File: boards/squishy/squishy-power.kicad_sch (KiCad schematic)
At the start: 63 parts, among them SW1 RST, U1 LFE5UM5G-45F-8BG381C, U10 TPS720115QDRVRQ1, U16 LP5910-1.8DRVR, U2 W25N01GVZEIG, U5 APX811-40UG-7, U7 TPS73733DRVR, U8 TPS7A1125PDRVT, U9 TPS7A1112PDRVT

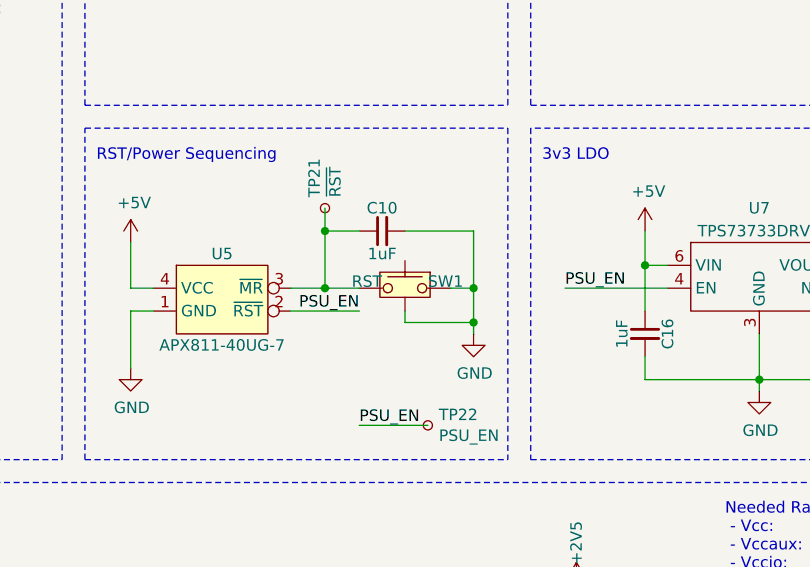
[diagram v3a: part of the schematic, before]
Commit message: hardware: squishy: some more minor work on the USB FE
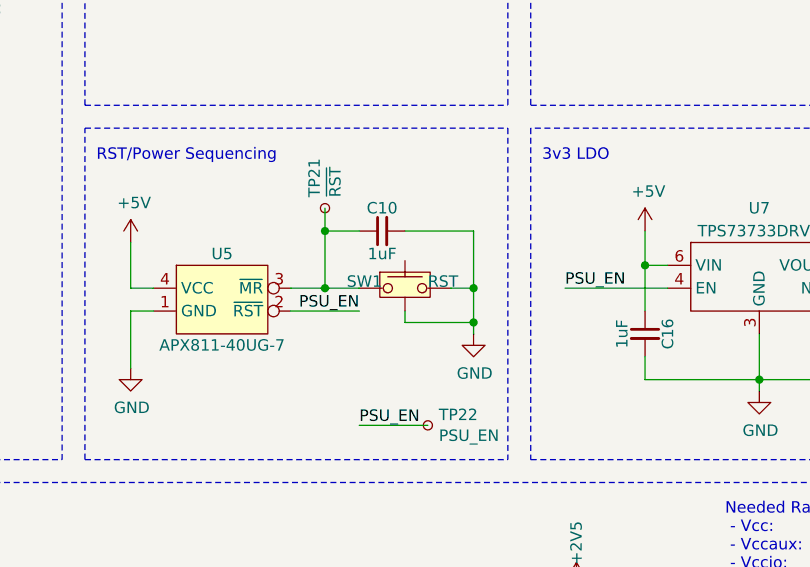
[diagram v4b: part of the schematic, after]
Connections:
- net GND: now also SW1.2; no longer SW1.1
- net at C10.1, TP21.1, U5.3 (~{MR}): now also SW1.1; no longer SW1.2
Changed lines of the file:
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@@
     (pin "2")
   )
-  (symbol (lib_id "lethalbit:SW_Push_Shield") (at 99.06 78.74 0) (mirror y) (unit 1)
+  (symbol (lib_id "lethalbit:SW_Push_Shield") (at 99.06 78.74 0) (unit 1)
     (in_bom yes) (on_board yes)
-    (property "Reference" "SW1" (id 0) (at 101.6 78.74 0)
+    (property "Reference" "SW1" (id 0) (at 96.52 78.74 0)
       (effects (font (size 1.27 1.27)) (justify right bottom))
     )
-    (property "Value" "RST" (id 1) (at 96.52 78.74 0)
+    (property "Value" "RST" (id 1) (at 101.6 78.74 0)
       (effects (font (size 1.27 1.27)) (justify left bottom))
     )

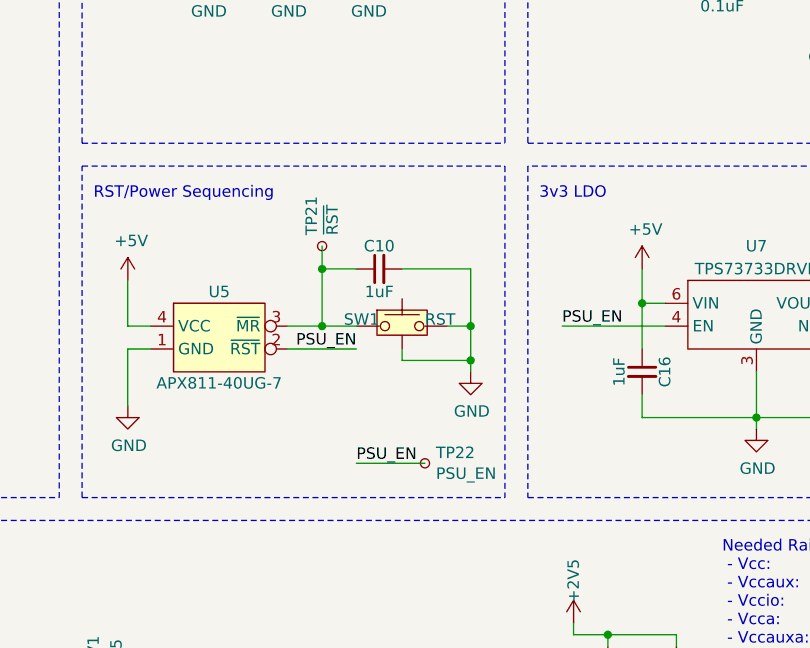
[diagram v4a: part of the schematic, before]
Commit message: hardware: squishy: cleaned up some testpoints and made sure things that should not be in the BOM are not
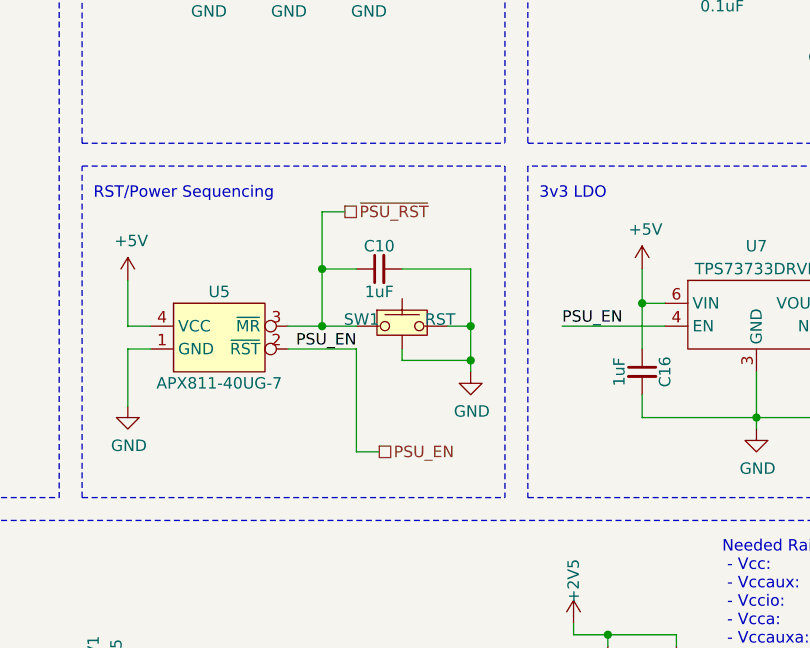
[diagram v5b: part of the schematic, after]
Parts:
- removed TP21: ~{RST}, TestPoint:TestPoint_Pad_D1.0mm, symbol Connector:TestPoint_Small
- removed TP22: PSU_EN, TestPoint:TestPoint_Pad_D1.0mm, symbol Connector:TestPoint_Small
- TP10, TP11, TP12, TP13, TP14, TP15, TP16, TP17, TP20, TP9: now left out of the parts list
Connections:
- net ~{PSU_RST}: now reaches C10.1, SW1.1, U5.3 (~{MR})
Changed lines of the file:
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@@
     (stroke (width 0) (type dash) (color 0 0 0 0))
+  )
+  (wire (pts (xy 90.17 66.04) (xy 92.71 66.04))
+    (stroke (width 0) (type default) (color 0 0 0 0))
   )
   (wire (pts (xy 130.81 130.81) (xy 130.81 129.54))
@@
     (stroke (width 0) (type solid) (color 0 0 0 0))
   )
+  (wire (pts (xy 90.17 66.04) (xy 90.17 72.39))
+    (stroke (width 0) (type default) (color 0 0 0 0))
+  )
   (wire (pts (xy 33.02 46.99) (xy 33.02 53.34))
     (stroke (width 0) (type solid) (color 0 0 0 0))
@@
     (stroke (width 0) (type default) (color 0 0 0 0))
   )
+  (wire (pts (xy 93.98 92.71) (xy 96.52 92.71))
+    (stroke (width 0) (type default) (color 0 0 0 0))
+  )
   (wire (pts (xy 201.93 102.87) (xy 201.93 107.95))
     (stroke (width 0) (type default) (color 0 0 0 0))
@@
     (stroke (width 0) (type default) (color 0 0 0 0))
   )
+  (wire (pts (xy 93.98 81.28) (xy 93.98 92.71))
+    (stroke (width 0) (type default) (color 0 0 0 0))
+  )
   (wire (pts (xy 172.72 39.37) (xy 172.72 41.91))
     (stroke (width 0) (type default) (color 0 0 0 0))
@@
     (stroke (width 0) (type default) (color 0 0 0 0))
   )
-  (wire (pts (xy 90.17 72.39) (xy 90.17 69.85))
-    (stroke (width 0) (type default) (color 0 0 0 0))
-  )
   (wire (pts (xy 187.96 166.37) (xy 187.96 168.91))
     (stroke (width 0) (type solid) (color 0 0 0 0))
@@
   )
   (wire (pts (xy 184.15 76.2) (xy 184.15 81.28))
-    (stroke (width 0) (type default) (color 0 0 0 0))
-  )
-  (wire (pts (xy 101.6 93.98) (xy 93.98 93.98))
     (stroke (width 0) (type default) (color 0 0 0 0))
   )
@@
     (effects (font (size 1.27 1.27)) (justify right bottom))
   )
-  (label "PSU_EN" (at 93.98 93.98 0)
-    (effects (font (size 1.27 1.27)) (justify left bottom))
-  )
   (label "PSU_EN" (at 116.84 78.74 0)
     (effects (font (size 1.27 1.27)) (justify left bottom))
@@
   (label "PSU_EN" (at 163.83 158.75 0)
     (effects (font (size 1.27 1.27)) (justify left bottom))
+  )
+  (hierarchical_label "~{PSU_RST}" (shape passive) (at 92.71 66.04 0)
+    (effects (font (size 1.27 1.27)) (justify left))
+  )
+  (hierarchical_label "PSU_EN" (shape passive) (at 96.52 92.71 0)
+    (effects (font (size 1.27 1.27)) (justify left))
   )
   (symbol (lib_id "Device:C_Small") (at 95.25 34.29 0) (unit 1)
@@
     (pin "1")
     (pin "2")
-  )
-  (symbol (lib_id "Connector:TestPoint_Small") (at 90.17 69.85 90) (unit 1)
-    (in_bom yes) (on_board yes)
-    (property "Reference" "TP21" (id 0) (at 89.0016 68.6308 0)
-      (effects (font (size 1.27 1.27)) (justify left))
-    )
-    (property "Value" "~{RST}" (id 1) (at 91.313 68.6308 0)
-      (effects (font (size 1.27 1.27)) (justify left))
-    )
-    (property "Footprint" "TestPoint:TestPoint_Pad_D1.0mm" (id 2) (at 90.17 64.77 0)
-      (effects (font (size 1.27 1.27)) hide)
-    )
-    (property "Datasheet" "~" (id 3) (at 90.17 64.77 0)
-      (effects (font (size 1.27 1.27)) hide)
-    )
-    (property "MFR" "N/A" (id 4) (at 90.17 69.85 0)
-      (effects (font (size 1.27 1.27)) hide)
-    )
-    (property "MPN" "N/A" (id 5) (at 90.17 69.85 0)
-      (effects (font (size 1.27 1.27)) hide)
-    )
-    (pin "1")
   )
   (symbol (lib_id "power:+1V1") (at 64.77 120.65 0) (unit 1)
@@
   )
   (symbol (lib_id "Connector:TestPoint_Small") (at 38.1 93.98 0) (unit 1)
-    (in_bom yes) (on_board yes)
+    (in_bom no) (on_board yes)
     (property "Reference" "TP17" (id 0) (at 39.3192 92.8116 0)
       (effects (font (size 1.27 1.27)) (justify left))
@@
   )
   (symbol (lib_id "Connector:TestPoint_Small") (at 38.1 48.26 0) (unit 1)
-    (in_bom yes) (on_board yes)
+    (in_bom no) (on_board yes)
     (property "Reference" "TP9" (id 0) (at 39.3192 47.0916 0)
       (effects (font (size 1.27 1.27)) (justify left))
@@
   )
   (symbol (lib_id "Connector:TestPoint_Small") (at 38.1 73.66 0) (unit 1)
-    (in_bom yes) (on_board yes)
+    (in_bom no) (on_board yes)
     (property "Reference" "TP13" (id 0) (at 39.3192 72.4916 0)
       (effects (font (size 1.27 1.27)) (justify left))
@@
   )
   (symbol (lib_id "Connector:TestPoint_Small") (at 38.1 53.34 0) (unit 1)
-    (in_bom yes) (on_board yes)
+    (in_bom no) (on_board yes)
     (property "Reference" "TP10" (id 0) (at 39.3192 52.1716 0)
       (effects (font (size 1.27 1.27)) (justify left))
@@
   )
   (symbol (lib_id "Connector:TestPoint_Small") (at 38.1 63.5 0) (unit 1)
-    (in_bom yes) (on_board yes)
+    (in_bom no) (on_board yes)
     (property "Reference" "TP12" (id 0) (at 39.3192 62.3316 0)
       (effects (font (size 1.27 1.27)) (justify left))
@@
     (pin "2")
   )
-  (symbol (lib_id "Connector:TestPoint_Small") (at 101.6 93.98 0) (unit 1)
-    (in_bom yes) (on_board yes)
-    (property "Reference" "TP22" (id 0) (at 102.8192 92.8116 0)
-      (effects (font (size 1.27 1.27)) (justify left))
-    )
-    (property "Value" "PSU_EN" (id 1) (at 102.8192 95.123 0)
-      (effects (font (size 1.27 1.27)) (justify left))
-    )
-    (property "Footprint" "TestPoint:TestPoint_Pad_D1.0mm" (id 2) (at 106.68 93.98 0)
-      (effects (font (size 1.27 1.27)) hide)
-    )
-    (property "Datasheet" "~" (id 3) (at 106.68 93.98 0)
-      (effects (font (size 1.27 1.27)) hide)
-    )
-    (property "MFR" "N/A" (id 4) (at 101.6 93.98 0)
-      (effects (font (size 1.27 1.27)) hide)
-    )
-    (property "MPN" "N/A" (id 5) (at 101.6 93.98 0)
-      (effects (font (size 1.27 1.27)) hide)
-    )
-    (pin "1")
-  )
   (symbol (lib_id "power:+2V5") (at 77.47 29.21 0) (unit 1)
     (in_bom yes) (on_board yes)
@@
   )
   (symbol (lib_id "Connector:TestPoint_Small") (at 38.1 68.58 0) (unit 1)
-    (in_bom yes) (on_board yes)
+    (in_bom no) (on_board yes)
     (property "Reference" "TP20" (id 0) (at 39.3192 67.4116 0)
       (effects (font (size 1.27 1.27)) (justify left))
@@
   )
   (symbol (lib_id "Connector:TestPoint_Small") (at 38.1 88.9 0) (unit 1)
-    (in_bom yes) (on_board yes)
+    (in_bom no) (on_board yes)
     (property "Reference" "TP16" (id 0) (at 39.3192 87.7316 0)
       (effects (font (size 1.27 1.27)) (justify left))
@@
   )
   (symbol (lib_id "Connector:TestPoint_Small") (at 38.1 78.74 0) (unit 1)
-    (in_bom yes) (on_board yes)
+    (in_bom no) (on_board yes)
     (property "Reference" "TP14" (id 0) (at 39.3192 77.5716 0)
       (effects (font (size 1.27 1.27)) (justify left))
@@
   )
   (symbol (lib_id "Connector:TestPoint_Small") (at 38.1 58.42 0) (unit 1)
-    (in_bom yes) (on_board yes)
+    (in_bom no) (on_board yes)
     (property "Reference" "TP11" (id 0) (at 39.3192 57.2516 0)
       (effects (font (size 1.27 1.27)) (justify left))
@@
   )
   (symbol (lib_id "Connector:TestPoint_Small") (at 38.1 83.82 0) (unit 1)
-    (in_bom yes) (on_board yes)
+    (in_bom no) (on_board yes)
     (property "Reference" "TP15" (id 0) (at 39.3192 82.6516 0)
       (effects (font (size 1.27 1.27)) (justify left))

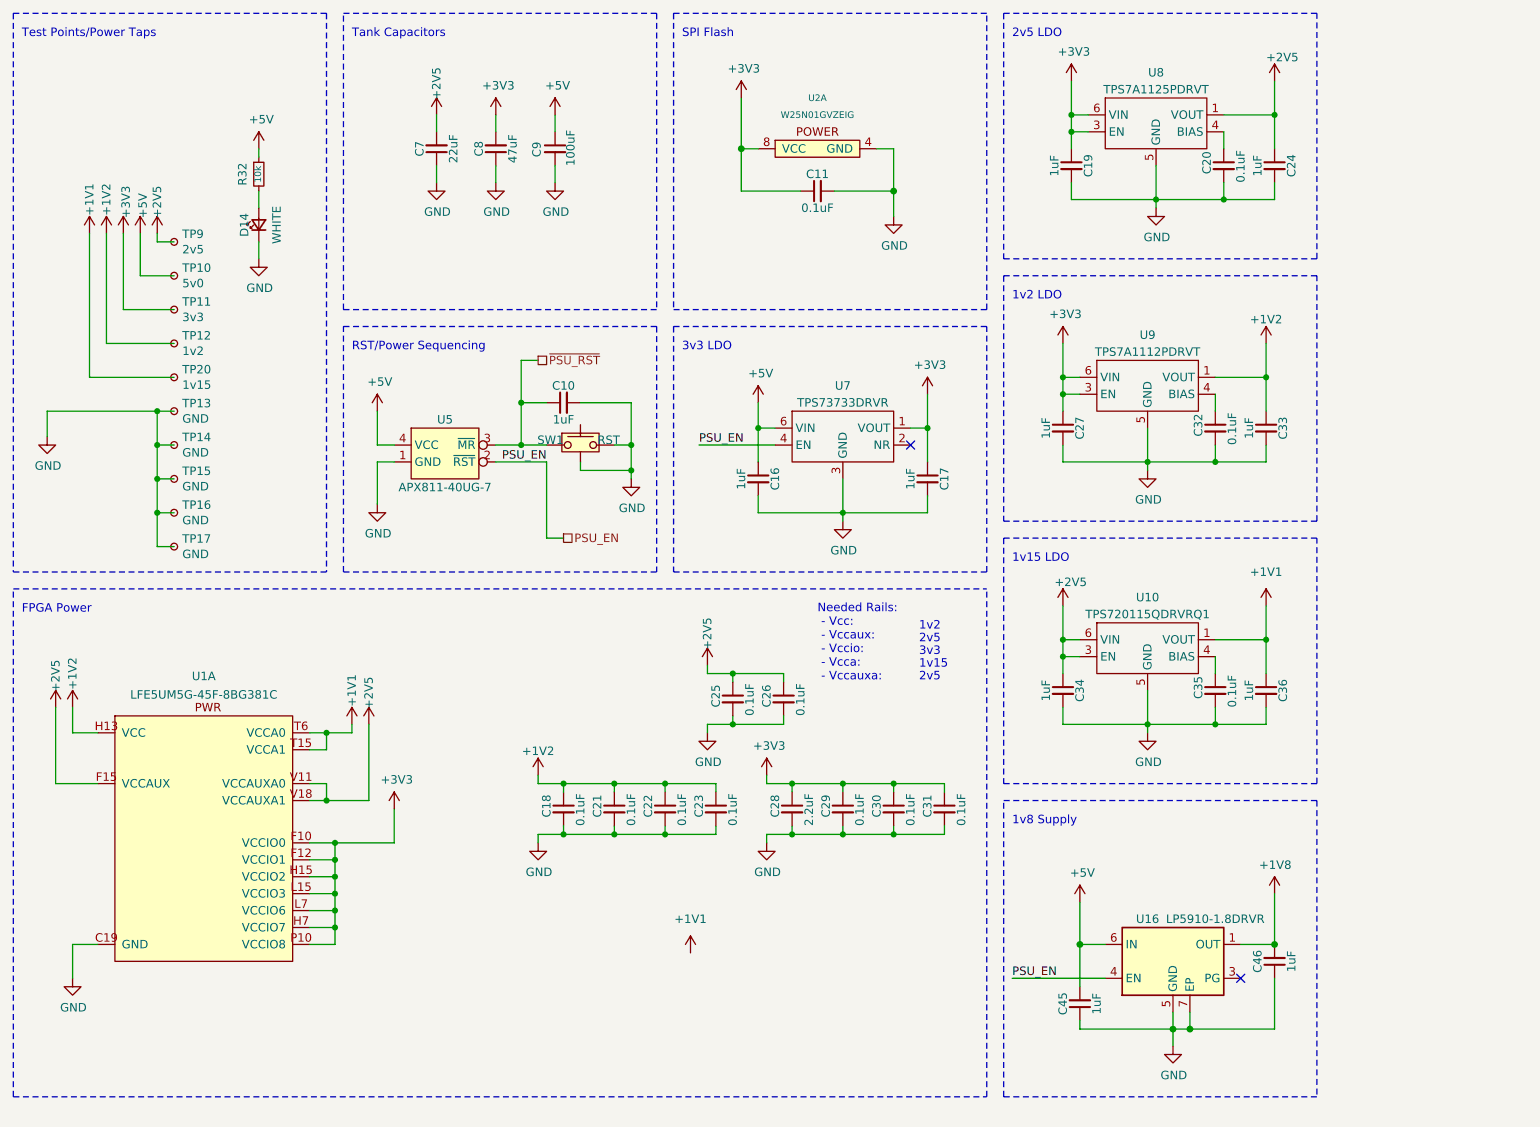
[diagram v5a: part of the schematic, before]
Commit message: hardware: squishy: some more cleanup, as well as starting work on the PSU side of things finally
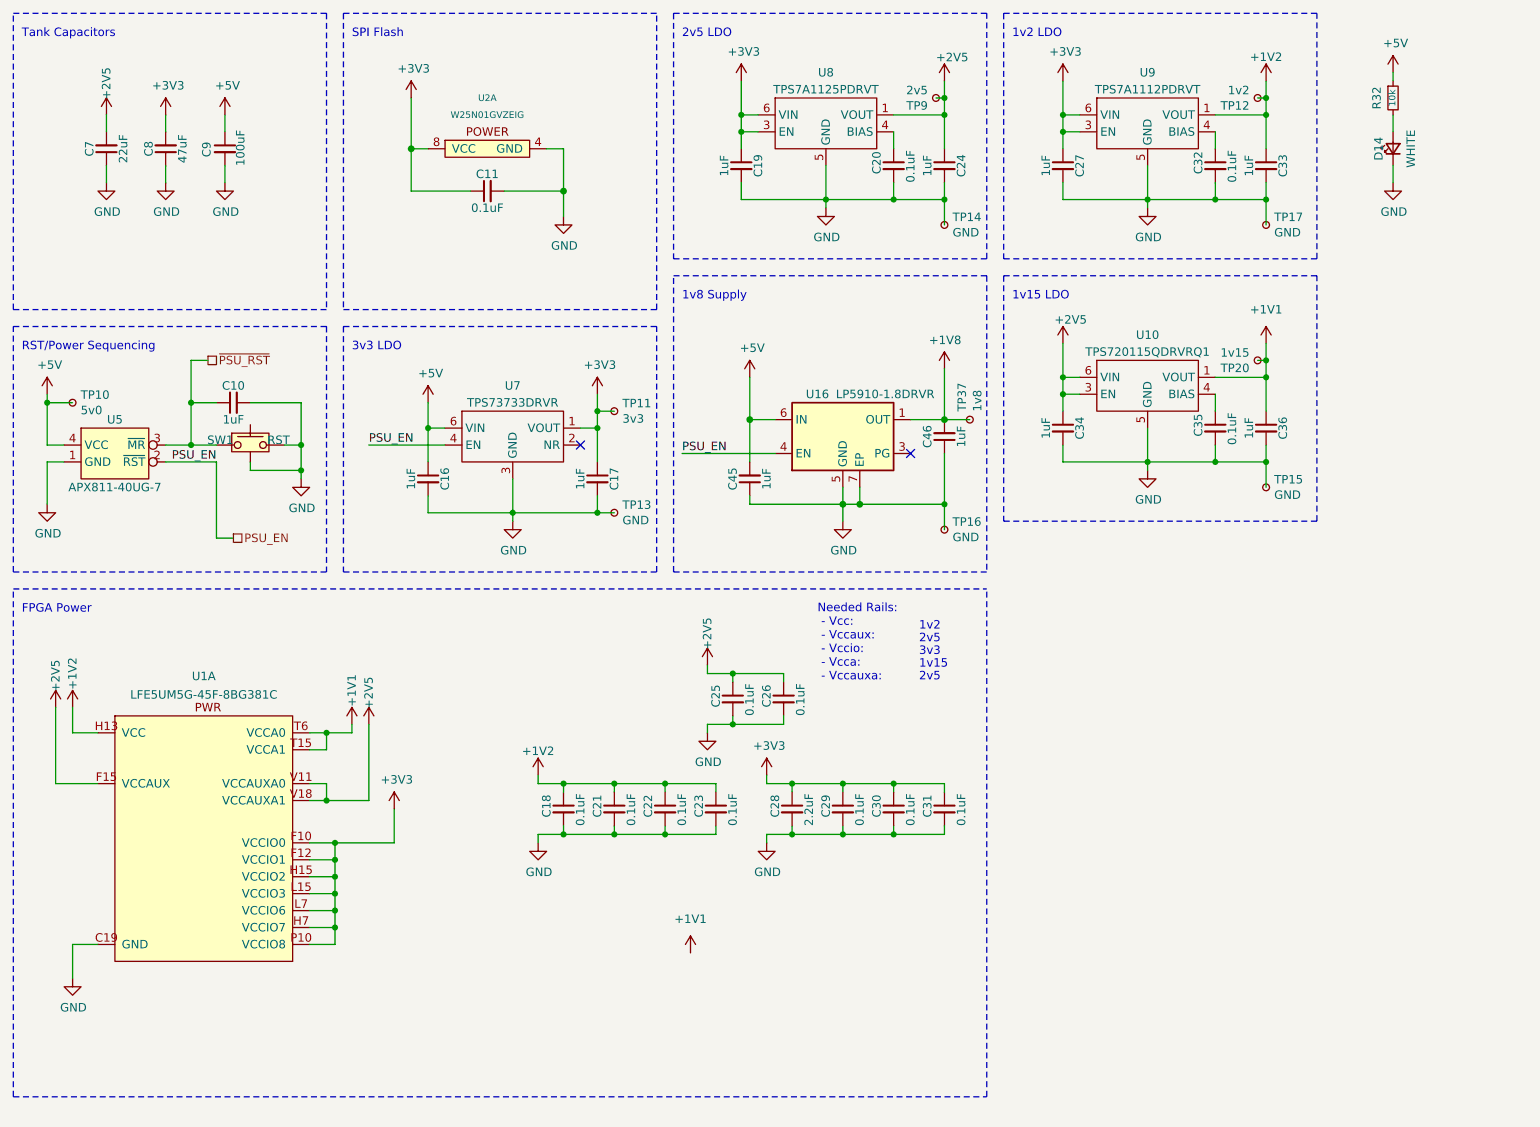
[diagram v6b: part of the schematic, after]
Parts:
- added TP37: 1v8, TestPoint:TestPoint_Pad_D1.0mm, symbol Connector:TestPoint_Small
- U5: footprint Package_TO_SOT_SMD:SOT-143 -> rhais_package-smd:SOT-143
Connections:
- net +1V8: now also TP37.1
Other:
- note removed: "Test Points/Power Taps"
- moved on the sheet: C10, C11, C16, C17, C19, C20, C24, C27, C32, C33, C34, C35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

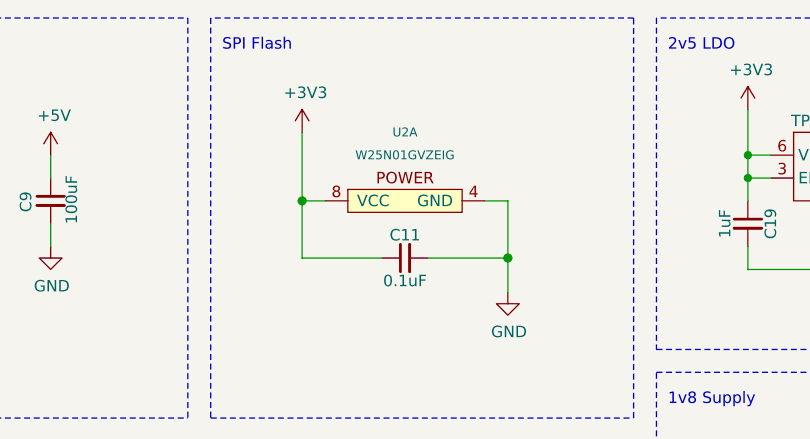
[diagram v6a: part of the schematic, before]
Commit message: hardware: squishy: replaced the SPI flash with a less batshit device from GigaDevice
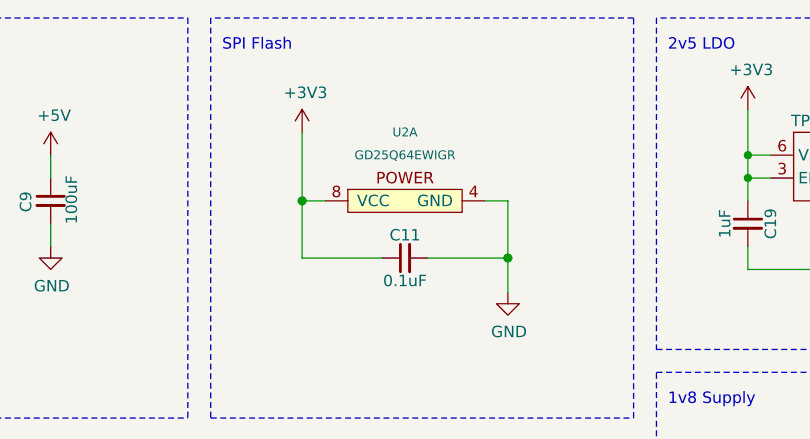
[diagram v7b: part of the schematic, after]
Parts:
- U2: value W25N01GVZEIG -> GD25Q64EWIGR; footprint lethalbit-memory:WSON-8-1EP-6.0x8.0mm -> Package_SON:WSON-8-1EP_6x5mm_P1.27mm_EP3.4x4mm; MFR Winbond -> GigaDevice; MPN W25N01GVZEIG TR -> GD25Q64EWIGR
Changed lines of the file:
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@@
       (effects (font (size 0.9906 0.9906)))
     )
-    (property "Value" "W25N01GVZEIG" (id 1) (at 85.09 29.21 0)
+    (property "Value" "GD25Q64EWIGR" (id 1) (at 85.09 29.21 0)
       (effects (font (size 0.9906 0.9906)))
     )
-    (property "Footprint" "lethalbit-memory:WSON-8-1EP-6.0x8.0mm" (id 2) (at 85.09 29.21 0)
+    (property "Footprint" "Package_SON:WSON-8-1EP_6x5mm_P1.27mm_EP3.4x4mm" (id 2) (at 85.09 29.21 0)
       (effects (font (size 0.9906 0.9906)) hide)
     )
-    (property "Datasheet" "https://www.winbond.com/resource-files/w25n01gv%20revl%20050918%20unsecured.pdf" (id 3) (at 85.09 29.21 0)
+    (property "Datasheet" "https://www.gigadevice.com/datasheet/GD25Q64E/" (id 3) (at 85.09 29.21 0)
       (effects (font (size 0.9906 0.9906)) hide)
     )
-    (property "MFR" "Winbond" (id 4) (at 85.09 33.02 0)
+    (property "MFR" "GigaDevice" (id 4) (at 85.09 33.02 0)
       (effects (font (size 1.27 1.27)) hide)
     )
-    (property "MPN" "W25N01GVZEIG TR" (id 5) (at 85.09 33.02 0)
+    (property "MPN" "GD25Q64EWIGR" (id 5) (at 85.09 33.02 0)
       (effects (font (size 1.27 1.27)) hide)
     )
